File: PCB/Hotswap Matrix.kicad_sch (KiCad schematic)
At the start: 96 parts, among them K1 KEYSW, K10 KEYSW, K11 KEYSW, K12 KEYSW, K13 KEYSW, K14 KEYSW, K15 KEYSW, K16 KEYSW, K17 KEYSW, K18 KEYSW, K19 KEYSW, K2 KEYSW, K20 KEYSW, K21 KEYSW, K22 KEYSW, K23 KEYSW, K24 KEYSW, K25 KEYSW, K26 KEYSW, K27 KEYSW, K28 KEYSW, K29 KEYSW, K3 KEYSW, K30 KEYSW, K31 KEYSW, K32 KEYSW, K33 KEYSW, K34 KEYSW, K35 KEYSW, K36 KEYSW, K37 KEYSW, K38 KEYSW, K39 KEYSW, K4 KEYSW, K40 KEYSW, K41 KEYSW, K42 KEYSW, K43 KEYSW, K44 KEYSW, K45 KEYSW, K46 KEYSW, K47 KEYSW, K5 KEYSW, K6 KEYSW, K7 KEYSW, K8 KEYSW, K9 KEYSW, SW1 RotaryEncoder_Switch

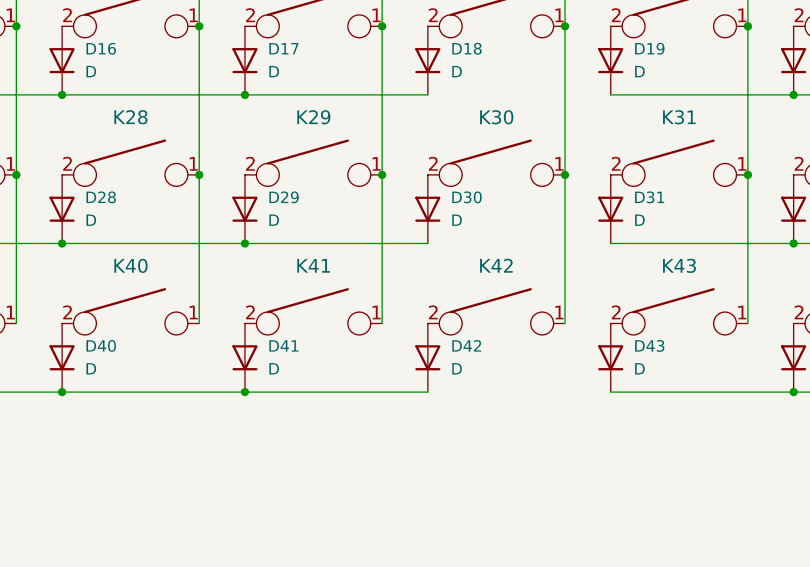
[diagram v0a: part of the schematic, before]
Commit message: Fixed a problem PCB Matrixes not being seperate. Uploaded somewhat broken ZMK firmware
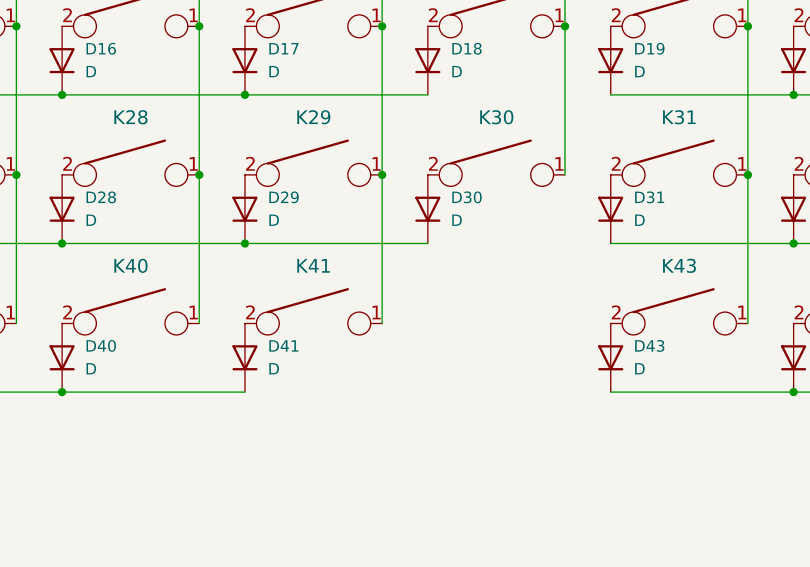
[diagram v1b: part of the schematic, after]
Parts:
- removed D42: D, Keebio:Diode-Hybrid-Back, symbol Device:D
- removed K42: KEYSW, mx footprints:MXOnly-1.25U-NoLED, symbol keyboard_parts:KEYSW
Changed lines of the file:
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@@
   (junction (at 111.76 83.82) (diameter 0.9144) (color 0 0 0 0))
   (junction (at 111.76 100.33) (diameter 0.9144) (color 0 0 0 0))
-  (junction (at 111.76 116.84) (diameter 0.9144) (color 0 0 0 0))
   (junction (at 127 59.69) (diameter 0.9144) (color 0 0 0 0))
   (junction (at 127 76.2) (diameter 0.9144) (color 0 0 0 0))
@@
   (junction (at 147.32 59.69) (diameter 0.9144) (color 0 0 0 0))
   (junction (at 147.32 76.2) (diameter 0.9144) (color 0 0 0 0))
-  (junction (at 147.32 92.71) (diameter 0.9144) (color 0 0 0 0))
   (junction (at 167.64 59.69) (diameter 0.9144) (color 0 0 0 0))
   (junction (at 167.64 76.2) (diameter 0.9144) (color 0 0 0 0))
@@
     (stroke (width 0) (type solid) (color 0 0 0 0))
   )
-  (wire (pts (xy 111.76 116.84) (xy 132.08 116.84))
-    (stroke (width 0) (type solid) (color 0 0 0 0))
-  )
   (wire (pts (xy 127 49.53) (xy 127 59.69))
     (stroke (width 0) (type solid) (color 0 0 0 0))
@@
   )
   (wire (pts (xy 147.32 76.2) (xy 147.32 92.71))
-    (stroke (width 0) (type solid) (color 0 0 0 0))
-  )
-  (wire (pts (xy 147.32 92.71) (xy 147.32 109.22))
     (stroke (width 0) (type solid) (color 0 0 0 0))
   )
@@
     (pin "2")
   )
-  (symbol (lib_id "Device:D") (at 132.08 113.03 90) (unit 1)
-    (in_bom yes) (on_board yes) (fields_autoplaced)
-    (property "Reference" "D42" (id 0) (at 134.62 111.7599 90)
-      (effects (font (size 1.27 1.27)) (justify right))
-    )
-    (property "Value" "D" (id 1) (at 134.62 114.2999 90)
-      (effects (font (size 1.27 1.27)) (justify right))
-    )
-    (property "Footprint" "Keebio:Diode-Hybrid-Back" (id 2) (at 132.08 113.03 0)
-      (effects (font (size 1.27 1.27)) hide)
-    )
-    (property "Datasheet" "~" (id 3) (at 132.08 113.03 0)
-      (effects (font (size 1.27 1.27)) hide)
-    )
-    (pin "1")
-    (pin "2")
-  )
   (symbol (lib_id "Device:D") (at 152.4 63.5 90) (unit 1)
     (in_bom yes) (on_board yes) (fields_autoplaced)
@@
       (effects (font (size 1.524 1.524)))
     )
-    (pin "1")
-    (pin "2")
-  )
-  (symbol (lib_id "keyboard_parts:KEYSW") (at 139.7 109.22 0) (unit 1)
-    (in_bom yes) (on_board yes) (fields_autoplaced)
-    (property "Reference" "K42" (id 0) (at 139.7 102.87 0)
-      (effects (font (size 1.524 1.524)))
-    )
-    (property "Value" "KEYSW" (id 1) (at 139.7 111.76 0)
-      (effects (font (size 1.524 1.524)) hide)
-    )
-    (property "Footprint" "mx footprints:MXOnly-1.25U-NoLED" (id 2) (at 139.7 109.22 0)
-      (effects (font (size 1.524 1.524)) hide)
-    )
-    (property "Datasheet" "" (id 3) (at 139.7 109.22 0)
-      (effects (font (size 1.524 1.524)))
-    )

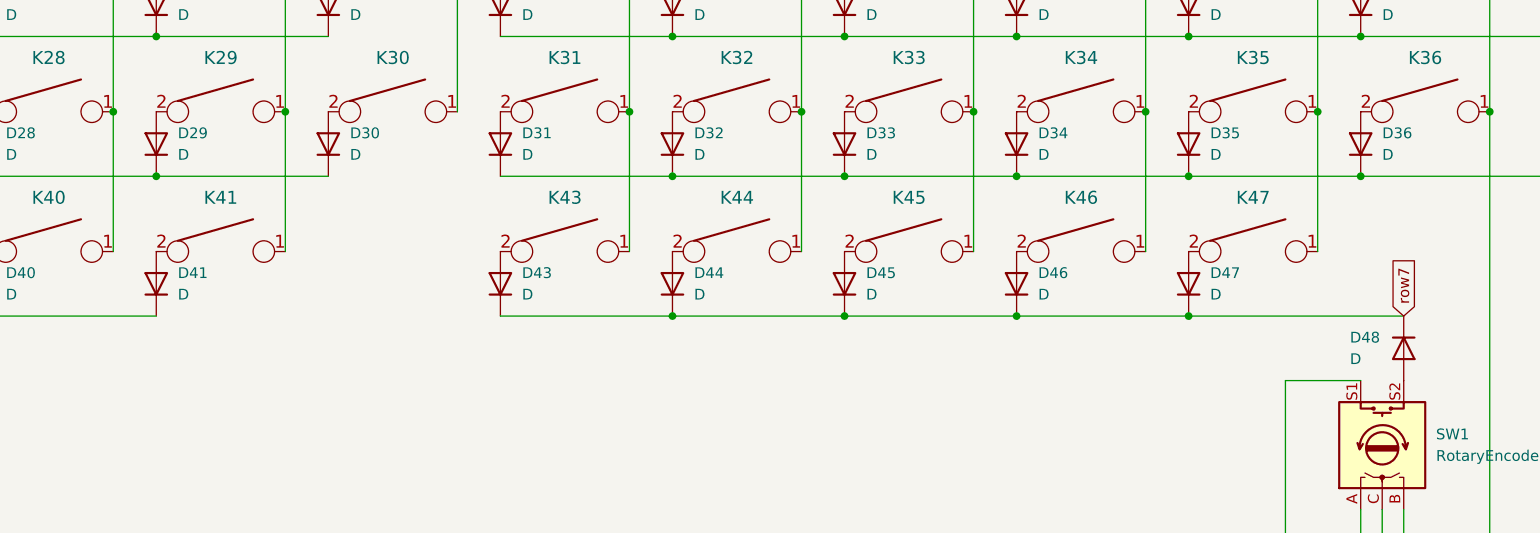
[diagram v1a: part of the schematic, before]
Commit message: Added battery hole to CNC case. Fixed odd linkages with kicad files. General firmware updates
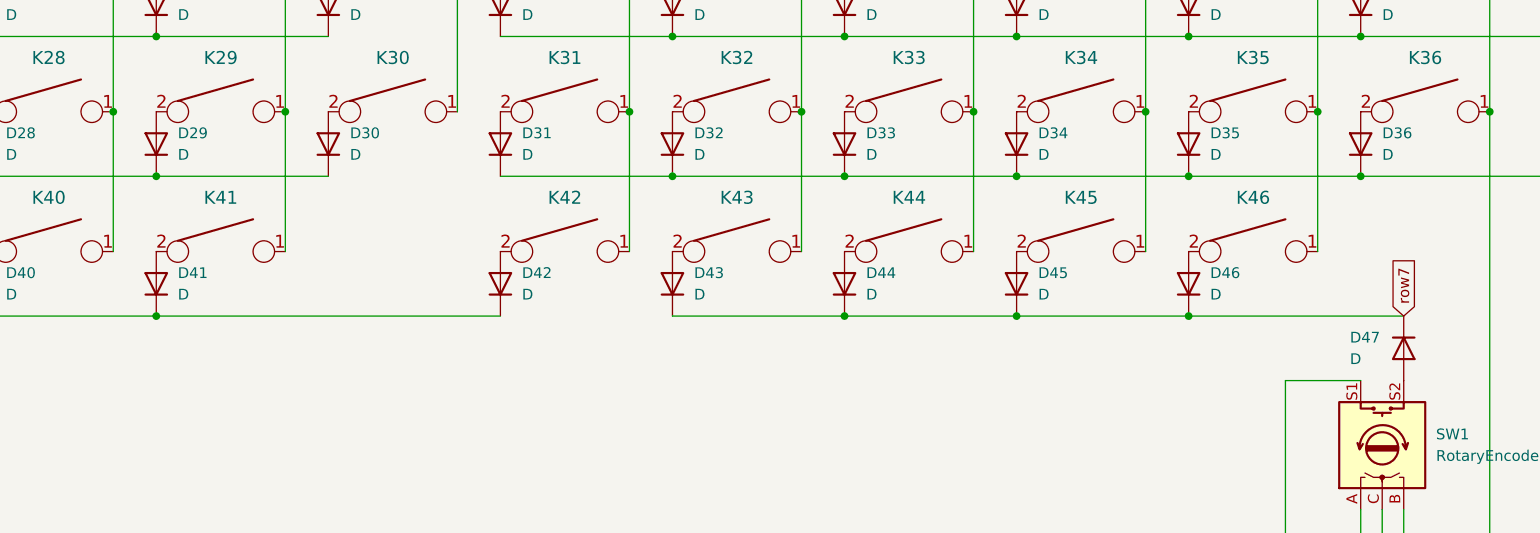
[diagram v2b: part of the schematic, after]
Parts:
- renumbered D43 to D42, D44 to D43, D45 to D44, D46 to D45, D47 to D46, D48 to D47, K43 to K42, K44 to K43, K45 to K44, K46 to K45, K47 to K46
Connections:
- net row3: now also D42.1 (K)
- net row7: no longer D42.1 (K)
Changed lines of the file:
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@@
   (junction (at 111.76 83.82) (diameter 0.9144) (color 0 0 0 0))
   (junction (at 111.76 100.33) (diameter 0.9144) (color 0 0 0 0))
+  (junction (at 111.76 116.84) (diameter 0.9144) (color 0 0 0 0))
   (junction (at 127 59.69) (diameter 0.9144) (color 0 0 0 0))
   (junction (at 127 76.2) (diameter 0.9144) (color 0 0 0 0))
@@
   (junction (at 172.72 83.82) (diameter 0.9144) (color 0 0 0 0))
   (junction (at 172.72 100.33) (diameter 0.9144) (color 0 0 0 0))
-  (junction (at 172.72 116.84) (diameter 0.9144) (color 0 0 0 0))
   (junction (at 187.96 59.69) (diameter 0.9144) (color 0 0 0 0))
   (junction (at 187.96 76.2) (diameter 0.9144) (color 0 0 0 0))
@@
     (stroke (width 0) (type solid) (color 0 0 0 0))
   )
+  (wire (pts (xy 111.76 116.84) (xy 152.4 116.84))
+    (stroke (width 0) (type solid) (color 0 0 0 0))
+  )
   (wire (pts (xy 127 49.53) (xy 127 59.69))
     (stroke (width 0) (type solid) (color 0 0 0 0))
@@
   )
   (wire (pts (xy 152.4 100.33) (xy 172.72 100.33))
-    (stroke (width 0) (type solid) (color 0 0 0 0))
-  )
-  (wire (pts (xy 152.4 116.84) (xy 172.72 116.84))
     (stroke (width 0) (type solid) (color 0 0 0 0))
   )
@@
   (symbol (lib_id "Device:D") (at 152.4 113.03 90) (unit 1)
     (in_bom yes) (on_board yes) (fields_autoplaced)
-    (property "Reference" "D43" (id 0) (at 154.94 111.7599 90)
+    (property "Reference" "D42" (id 0) (at 154.94 111.7599 90)
       (effects (font (size 1.27 1.27)) (justify right))
     )
@@
   (symbol (lib_id "Device:D") (at 172.72 113.03 90) (unit 1)
     (in_bom yes) (on_board yes) (fields_autoplaced)
-    (property "Reference" "D44" (id 0) (at 175.26 111.7599 90)
+    (property "Reference" "D43" (id 0) (at 175.26 111.7599 90)
       (effects (font (size 1.27 1.27)) (justify right))
     )
@@
   (symbol (lib_id "Device:D") (at 193.04 113.03 90) (unit 1)
     (in_bom yes) (on_board yes) (fields_autoplaced)
-    (property "Reference" "D45" (id 0) (at 195.58 111.7599 90)
+    (property "Reference" "D44" (id 0) (at 195.58 111.7599 90)
       (effects (font (size 1.27 1.27)) (justify right))
     )
@@
   (symbol (lib_id "Device:D") (at 213.36 113.03 90) (unit 1)
     (in_bom yes) (on_board yes) (fields_autoplaced)
-    (property "Reference" "D46" (id 0) (at 215.9 111.7599 90)
+    (property "Reference" "D45" (id 0) (at 215.9 111.7599 90)
       (effects (font (size 1.27 1.27)) (justify right))
     )
@@
   (symbol (lib_id "Device:D") (at 233.68 113.03 90) (unit 1)
     (in_bom yes) (on_board yes) (fields_autoplaced)
-    (property "Reference" "D47" (id 0) (at 236.22 111.7599 90)
+    (property "Reference" "D46" (id 0) (at 236.22 111.7599 90)
       (effects (font (size 1.27 1.27)) (justify right))
     )
@@
   (symbol (lib_id "Device:D") (at 259.08 120.65 270) (unit 1)
     (in_bom yes) (on_board yes)
-    (property "Reference" "D48" (id 0) (at 252.73 119.3799 90)
+    (property "Reference" "D47" (id 0) (at 252.73 119.3799 90)
       (effects (font (size 1.27 1.27)) (justify left))
     )
@@
   (symbol (lib_id "keyboard_parts:KEYSW") (at 160.02 109.22 0) (unit 1)
     (in_bom yes) (on_board yes) (fields_autoplaced)
-    (property "Reference" "K43" (id 0) (at 160.02 102.87 0)
+    (property "Reference" "K42" (id 0) (at 160.02 102.87 0)
       (effects (font (size 1.524 1.524)))
     )
@@
   (symbol (lib_id "keyboard_parts:KEYSW") (at 180.34 109.22 0) (unit 1)
     (in_bom yes) (on_board yes) (fields_autoplaced)
-    (property "Reference" "K44" (id 0) (at 180.34 102.87 0)
+    (property "Reference" "K43" (id 0) (at 180.34 102.87 0)
       (effects (font (size 1.524 1.524)))
     )
@@
   (symbol (lib_id "keyboard_parts:KEYSW") (at 200.66 109.22 0) (unit 1)
     (in_bom yes) (on_board yes) (fields_autoplaced)
-    (property "Reference" "K45" (id 0) (at 200.66 102.87 0)
+    (property "Reference" "K44" (id 0) (at 200.66 102.87 0)
       (effects (font (size 1.524 1.524)))
     )
@@
   (symbol (lib_id "keyboard_parts:KEYSW") (at 220.98 109.22 0) (unit 1)
     (in_bom yes) (on_board yes) (fields_autoplaced)
-    (property "Reference" "K46" (id 0) (at 220.98 102.87 0)
+    (property "Reference" "K45" (id 0) (at 220.98 102.87 0)
       (effects (font (size 1.524 1.524)))
     )
@@
   (symbol (lib_id "keyboard_parts:KEYSW") (at 241.3 109.22 0) (unit 1)
     (in_bom yes) (on_board yes) (fields_autoplaced)
-    (property "Reference" "K47" (id 0) (at 241.3 102.87 0)
-      (effects (font (size 1.524 1.524)))
-    )
+    (property "Reference" "K46" (id 0) (at 241.3 102.87 0)
+      (effects (font (size 1.524 1.524)))
+    )

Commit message: Second revision for the IC
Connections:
- net row3: no longer D42.1 (K)
- net row7: now also D42.1 (K)
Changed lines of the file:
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@@
   (junction (at 111.76 83.82) (diameter 0.9144) (color 0 0 0 0))
   (junction (at 111.76 100.33) (diameter 0.9144) (color 0 0 0 0))
-  (junction (at 111.76 116.84) (diameter 0.9144) (color 0 0 0 0))
   (junction (at 127 59.69) (diameter 0.9144) (color 0 0 0 0))
   (junction (at 127 76.2) (diameter 0.9144) (color 0 0 0 0))
@@
   (junction (at 172.72 83.82) (diameter 0.9144) (color 0 0 0 0))
   (junction (at 172.72 100.33) (diameter 0.9144) (color 0 0 0 0))
+  (junction (at 172.72 116.84) (diameter 0.9144) (color 0 0 0 0))
   (junction (at 187.96 59.69) (diameter 0.9144) (color 0 0 0 0))
   (junction (at 187.96 76.2) (diameter 0.9144) (color 0 0 0 0))
@@
     (stroke (width 0) (type solid) (color 0 0 0 0))
   )
-  (wire (pts (xy 111.76 116.84) (xy 152.4 116.84))
-    (stroke (width 0) (type solid) (color 0 0 0 0))
-  )
   (wire (pts (xy 127 49.53) (xy 127 59.69))
     (stroke (width 0) (type solid) (color 0 0 0 0))
@@
     (stroke (width 0) (type solid) (color 0 0 0 0))
   )
+  (wire (pts (xy 152.4 116.84) (xy 172.72 116.84))
+    (stroke (width 0) (type solid) (color 0 0 0 0))
+  )
